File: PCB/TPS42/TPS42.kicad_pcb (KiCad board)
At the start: 2 copper layers, 138.1 x 89.7 mm, 77 parts, among them J1 PJ-320A, J11 Conn_01x06, J14 FH12-10S-0.5SH, J3 TP Sensor Module, J4 TP Module, J6 OLED, J7 TrackPoint, J8 Battery, J9 TP Sensor Module, SW1 SW_DPST_x2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

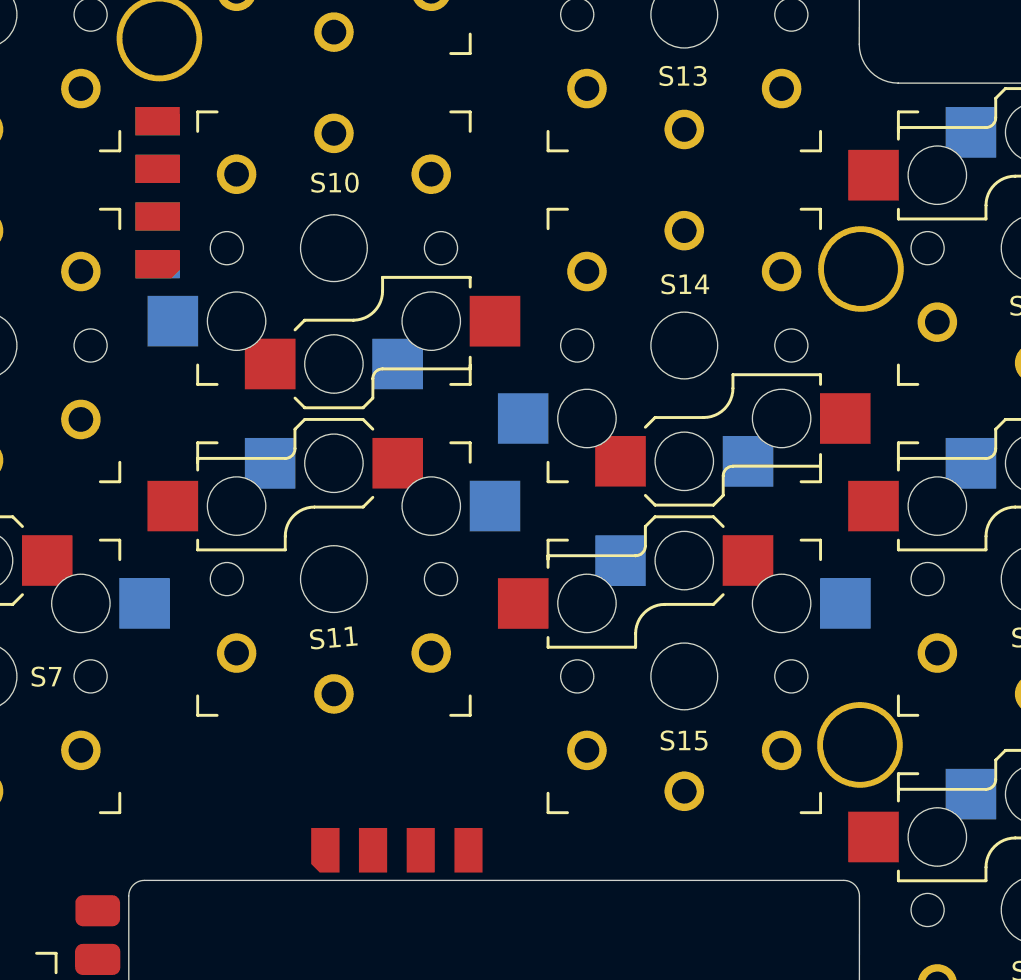
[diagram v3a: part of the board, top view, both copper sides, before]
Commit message: connected tp module
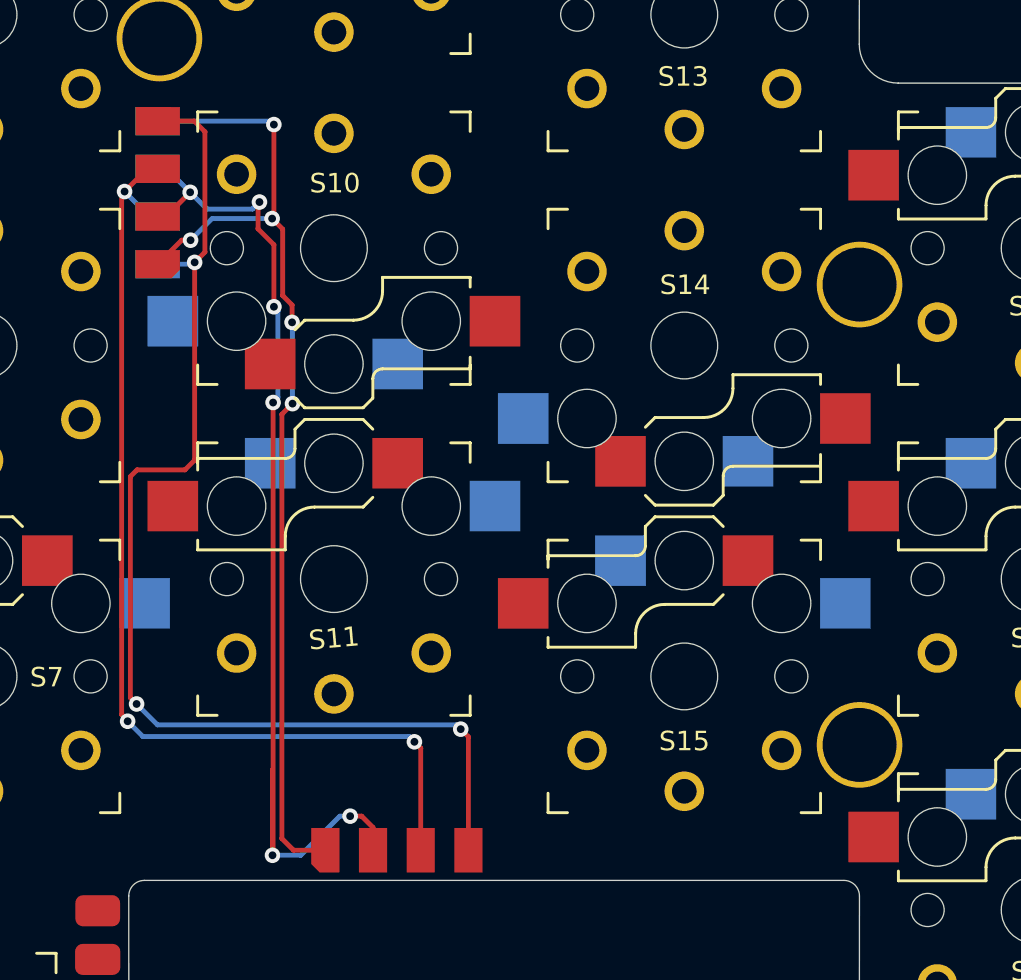
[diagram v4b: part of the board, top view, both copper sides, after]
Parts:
- moved U7 0.80 mm to (175.3, 62.6)
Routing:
- net Net-(J3-Pad4): track 0.00 -> 60.7 mm, vias 0 -> 3
- net Net-(J3-Pad2): track 0.00 -> 54.4 mm, vias 0 -> 6
- net Net-(J3-Pad3): track 0.00 -> 53.9 mm, vias 0 -> 3
- net Net-(J3-Pad1): track 0.00 -> 52.8 mm, vias 0 -> 5
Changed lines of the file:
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@@
   )
   (footprint "TPS42:HOLE_M2_TH" (layer "F.Cu")
-    (at 175.35 61.82)
+    (at 175.28 62.62)
     (property "Sheetfile" "TPS42.kicad_sch")
     (property "Sheetname" "")
@@
   )
   (footprint "TPS42:HOLE_M2_TH" (layer "F.Cu")
-    (at 175.3 86.27)
+    (at 175.28 86.27)
     (property "Sheetfile" "TPS42.kicad_sch")
     (property "Sheetname" "")
@@
     (effects (font (size 1 1) (thickness 0.15)))
   )
+  (segment (start 140.455 60.34) (end 139.22 61.575) (width 0.25) (layer "F.Cu") (net 44))
+  (segment (start 146.1245 63.667517) (end 145.641889 63.184906) (width 0.25) (layer "F.Cu") (net 44))
+  (segment (start 145.19 59.14) (end 145.1 59.23) (width 0.25) (layer "F.Cu") (net 44))
+  (segment (start 145.59952 69.285684) (end 145.59952 91.07952) (width 0.25) (layer "F.Cu") (net 44))
+  (segment (start 145.641889 59.771889) (end 145.1 59.23) (width 0.25) (layer "F.Cu") (net 44))
+  (segment (start 146.147856 68.737348) (end 145.59952 69.285684) (width 0.25) (layer "F.Cu") (net 44))
+  (segment (start 140.91 60.34) (end 140.455 60.34) (width 0.25) (layer "F.Cu") (net 44))
+  (segment (start 145.59952 91.07952) (end 146.2 91.68) (width 0.25) (layer "F.Cu") (net 44))
+  (segment (start 145.19 54.4) (end 145.19 59.14) (width 0.25) (layer "F.Cu") (net 44))
+  (segment (start 146.1245 64.56) (end 146.1245 63.667517) (width 0.25) (layer "F.Cu") (net 44))
+  (segment (start 146.2 91.68) (end 147.835 91.68) (width 0.25) (layer "F.Cu") (net 44))
+  (segment (start 145.641889 63.184906) (end 145.641889 59.771889) (width 0.25) (layer "F.Cu") (net 44))
+  (via (at 146.1245 64.56) (size 0.8) (drill 0.4) (layers "F.Cu" "B.Cu") (net 44))
+  (via (at 145.19 54.4) (size 0.8) (drill 0.4) (layers "F.Cu" "B.Cu") (net 44))
+  (via (at 140.91 60.34) (size 0.8) (drill 0.4) (layers "F.Cu" "B.Cu") (net 44))
+  (via (at 145.1 59.23) (size 0.8) (drill 0.4) (layers "F.Cu" "B.Cu") (net 44))
+  (via (at 146.147856 68.737348) (size 0.8) (drill 0.4) (layers "F.Cu" "B.Cu") (net 44))
+  (segment (start 145.015 54.225) (end 145.19 54.4) (width 0.25) (layer "B.Cu") (net 44))
+  (segment (start 142.02 59.23) (end 145.1 59.23) (width 0.25) (layer "B.Cu") (net 44))
+  (segment (start 139.22 54.225) (end 145.015 54.225) (width 0.25) (layer "B.Cu") (net 44))
+  (segment (start 140.91 60.34) (end 142.02 59.23) (width 0.25) (layer "B.Cu") (net 44))
+  (segment (start 146.14 68.729492) (end 146.14 64.5755) (width 0.25) (layer "B.Cu") (net 44))
+  (segment (start 146.14 64.5755) (end 146.1245 64.56) (width 0.25) (layer "B.Cu") (net 44))
+  (segment (start 146.147856 68.737348) (end 146.14 68.729492) (width 0.25) (layer "B.Cu") (net 44))
+  (segment (start 144.375489 58.454511) (end 144.45 58.38) (width 0.25) (layer "F.Cu") (net 45))
+  (segment (start 149.7 89.93) (end 150.285 90.515) (width 0.25) (layer "F.Cu") (net 45))
+  (segment (start 150.285 90.515) (end 150.285 91.68) (width 0.25) (layer "F.Cu") (net 45))
+  (segment (start 145.12 91.94) (end 145.12 87.53) (width 0.25) (layer "F.Cu") (net 45))
+  (segment (start 145.15 68.68) (end 145.15 91.91) (width 0.25) (layer "F.Cu") (net 45))
+  (segment (start 145.15 91.91) (end 145.12 91.94) (width 0.25) (layer "F.Cu") (net 45))
+  (segment (start 140.89 57.88) (end 139.645 59.125) (width 0.25) (layer "F.Cu") (net 45))
+  (segment (start 149.11 89.93) (end 149.7 89.93) (width 0.25) (layer "F.Cu") (net 45))
+  (segment (start 145.192369 60.572369) (end 144.375489 59.755489) (width 0.25) (layer "F.Cu") (net 45))
+  (segment (start 139.645 59.125) (end 139.22 59.125) (width 0.25) (layer "F.Cu") (net 45))
+  (segment (start 145.192369 63.76) (end 145.192369 60.572369) (width 0.25) (layer "F.Cu") (net 45))
+  (segment (start 144.375489 59.755489) (end 144.375489 58.454511) (width 0.25) (layer "F.Cu") (net 45))
+  (via (at 144.45 58.38) (size 0.8) (drill 0.4) (layers "F.Cu" "B.Cu") (net 45))
+  (via (at 145.192369 63.76) (size 0.8) (drill 0.4) (layers "F.Cu" "B.Cu") (net 45))
+  (via (at 140.89 57.88) (size 0.8) (drill 0.4) (layers "F.Cu" "B.Cu") (net 45))
+  (via (at 145.15 68.68) (size 0.8) (drill 0.4) (layers "F.Cu" "B.Cu") (net 45))
+  (via (at 145.12 91.94) (size 0.8) (drill 0.4) (layers "F.Cu" "B.Cu") (net 45))
+  (via (at 149.11 89.93) (size 0.8) (drill 0.4) (layers "F.Cu" "B.Cu") (net 45))
+  (segment (start 148.58 89.93) (end 146.57 91.94) (width 0.25) (layer "B.Cu") (net 45))
+  (segment (start 146.57 91.94) (end 145.12 91.94) (width 0.25) (layer "B.Cu") (net 45))
+  (segment (start 145.192369 63.76) (end 145.4 63.967631) (width 0.25) (layer "B.Cu") (net 45))
+  (segment (start 144.09 58.74) (end 144.45 58.38) (width 0.25) (layer "B.Cu") (net 45))
+  (segment (start 149.11 89.93) (end 148.58 89.93) (width 0.25) (layer "B.Cu") (net 45))
+  (segment (start 140.89 57.88) (end 141.75 58.74) (width 0.25) (layer "B.Cu") (net 45))
+  (segment (start 145.4 63.967631) (end 145.4 68.43) (width 0.25) (layer "B.Cu") (net 45))
+  (segment (start 141.75 58.74) (end 144.09 58.74) (width 0.25) (layer "B.Cu") (net 45))
+  (segment (start 139.685 56.675) (end 139.22 56.675) (width 0.25) (layer "B.Cu") (net 45))
+  (segment (start 145.4 68.43) (end 145.15 68.68) (width 0.25) (layer "B.Cu") (net 45))
+  (segment (start 140.89 57.88) (end 139.685 56.675) (width 0.25) (layer "B.Cu") (net 45))
+  (segment (start 139.865 56.675) (end 139.22 56.675) (width 0.25) (layer "F.Cu") (net 46))
+  (segment (start 152.41 86.11) (end 152.735 86.435) (width 0.25) (layer "F.Cu") (net 46))
+  (segment (start 137.37 57.99) (end 137.52 57.84) (width 0.25) (layer "F.Cu") (net 46))
+  (segment (start 137.37 84.708564) (end 137.37 57.99) (width 0.25) (layer "F.Cu") (net 46))
+  (segment (start 152.735 86.435) (end 152.735 91.68) (width 0.25) (layer "F.Cu") (net 46))
+  (segment (start 137.52 57.84) (end 138.685 56.675) (width 0.25) (layer "F.Cu") (net 46))
+  (segment (start 137.677064 85.015628) (end 137.37 84.708564) (width 0.25) (layer "F.Cu") (net 46))
+  (segment (start 138.685 56.675) (end 139.22 56.675) (width 0.25) (layer "F.Cu") (net 46))
+  (segment (start 137.677064 85.053399) (end 137.677064 85.015628) (width 0.25) (layer "F.Cu") (net 46))
+  (via (at 137.677064 85.053399) (size 0.8) (drill 0.4) (layers "F.Cu" "B.Cu") (net 46))
+  (via (at 137.52 57.84) (size 0.8) (drill 0.4) (layers "F.Cu" "B.Cu") (net 46))
+  (via (at 152.41 86.11) (size 0.8) (drill 0.4) (layers "F.Cu" "B.Cu") (net 46))
+  (segment (start 138.463665 85.84) (end 137.677064 85.053399) (width 0.25) (layer "B.Cu") (net 46))
+  (segment (start 138.805 59.125) (end 139.22 59.125) (width 0.25) (layer "B.Cu") (net 46))
+  (segment (start 152.41 86.11) (end 152.14 85.84) (width 0.25) (layer "B.Cu") (net 46))
+  (segment (start 152.14 85.84) (end 138.463665 85.84) (width 0.25) (layer "B.Cu") (net 46))
+  (segment (start 139.22 59.125) (end 139.825 59.125) (width 0.25) (layer "B.Cu") (net 46))
+  (segment (start 137.52 57.84) (end 138.805 59.125) (width 0.25) (layer "B.Cu") (net 46))
+  (segment (start 139.643 54.22) (end 141.1 54.22) (width 0.25) (layer "F.Cu") (net 47))
+  (segment (start 138.16 72.14) (end 140.62 72.14) (width 0.25) (layer "F.Cu") (net 47))
+  (segment (start 140.62 72.14) (end 141.12 71.64) (width 0.25) (layer "F.Cu") (net 47))
+  (segment (start 141.65 54.77) (end 141.65 60.95) (width 0.25) (layer "F.Cu") (net 47))
+  (segment (start 154.79 85.46) (end 155.185 85.855) (width 0.25) (layer "F.Cu") (net 47))
+  (segment (start 141.1 54.22) (end 141.65 54.77) (width 0.25) (layer "F.Cu") (net 47))
+  (segment (start 137.81952 83.848125) (end 137.81952 72.48048) (width 0.25) (layer "F.Cu") (net 47))
+  (segment (start 141.65 60.95) (end 141.12 61.48) (width 0.25) (layer "F.Cu") (net 47))
+  (segment (start 155.185 85.855) (end 155.185 91.68) (width 0.25) (layer "F.Cu") (net 47))
+  (segment (start 137.81952 72.48048) (end 138.16 72.14) (width 0.25) (layer "F.Cu") (net 47))
+  (segment (start 138.137836 84.166441) (end 137.81952 83.848125) (width 0.25) (layer "F.Cu") (net 47))
+  (segment (start 139.22 54.225) (end 139.638 54.225) (width 0.25) (layer "F.Cu") (net 47))
+  (segment (start 141.12 71.64) (end 141.12 61.48) (width 0.25) (layer "F.Cu") (net 47))
+  (segment (start 139.638 54.225) (end 139.643 54.22) (width 0.25) (layer "F.Cu") (net 47))
+  (via (at 154.79 85.46) (size 0.8) (drill 0.4) (layers "F.Cu" "B.Cu") (net 47))
+  (via (at 141.12 61.48) (size 0.8) (drill 0.4) (layers "F.Cu" "B.Cu") (net 47))
+  (via (at 138.137836 84.166441) (size 0.8) (drill 0.4) (layers "F.Cu" "B.Cu") (net 47))
+  (segment (start 154.57 85.24) (end 139.211395 85.24) (width 0.25) (layer "B.Cu") (net 47))
+  (segment (start 154.79 85.46) (end 154.57 85.24) (width 0.25) (layer "B.Cu") (net 47))
+  (segment (start 139.22 61.575) (end 141.025 61.575) (width 0.25) (layer "B.Cu") (net 47))
+  (segment (start 139.211395 85.24) (end 138.137836 84.166441) (width 0.25) (layer "B.Cu") (net 47))
+  (segment (start 141.025 61.575) (end 141.12 61.48) (width 0.25) (layer "B.Cu") (net 47))
   (group "" (id 50fe513a-550e-4e47-b3e6-31ef45e7540b)
     (members

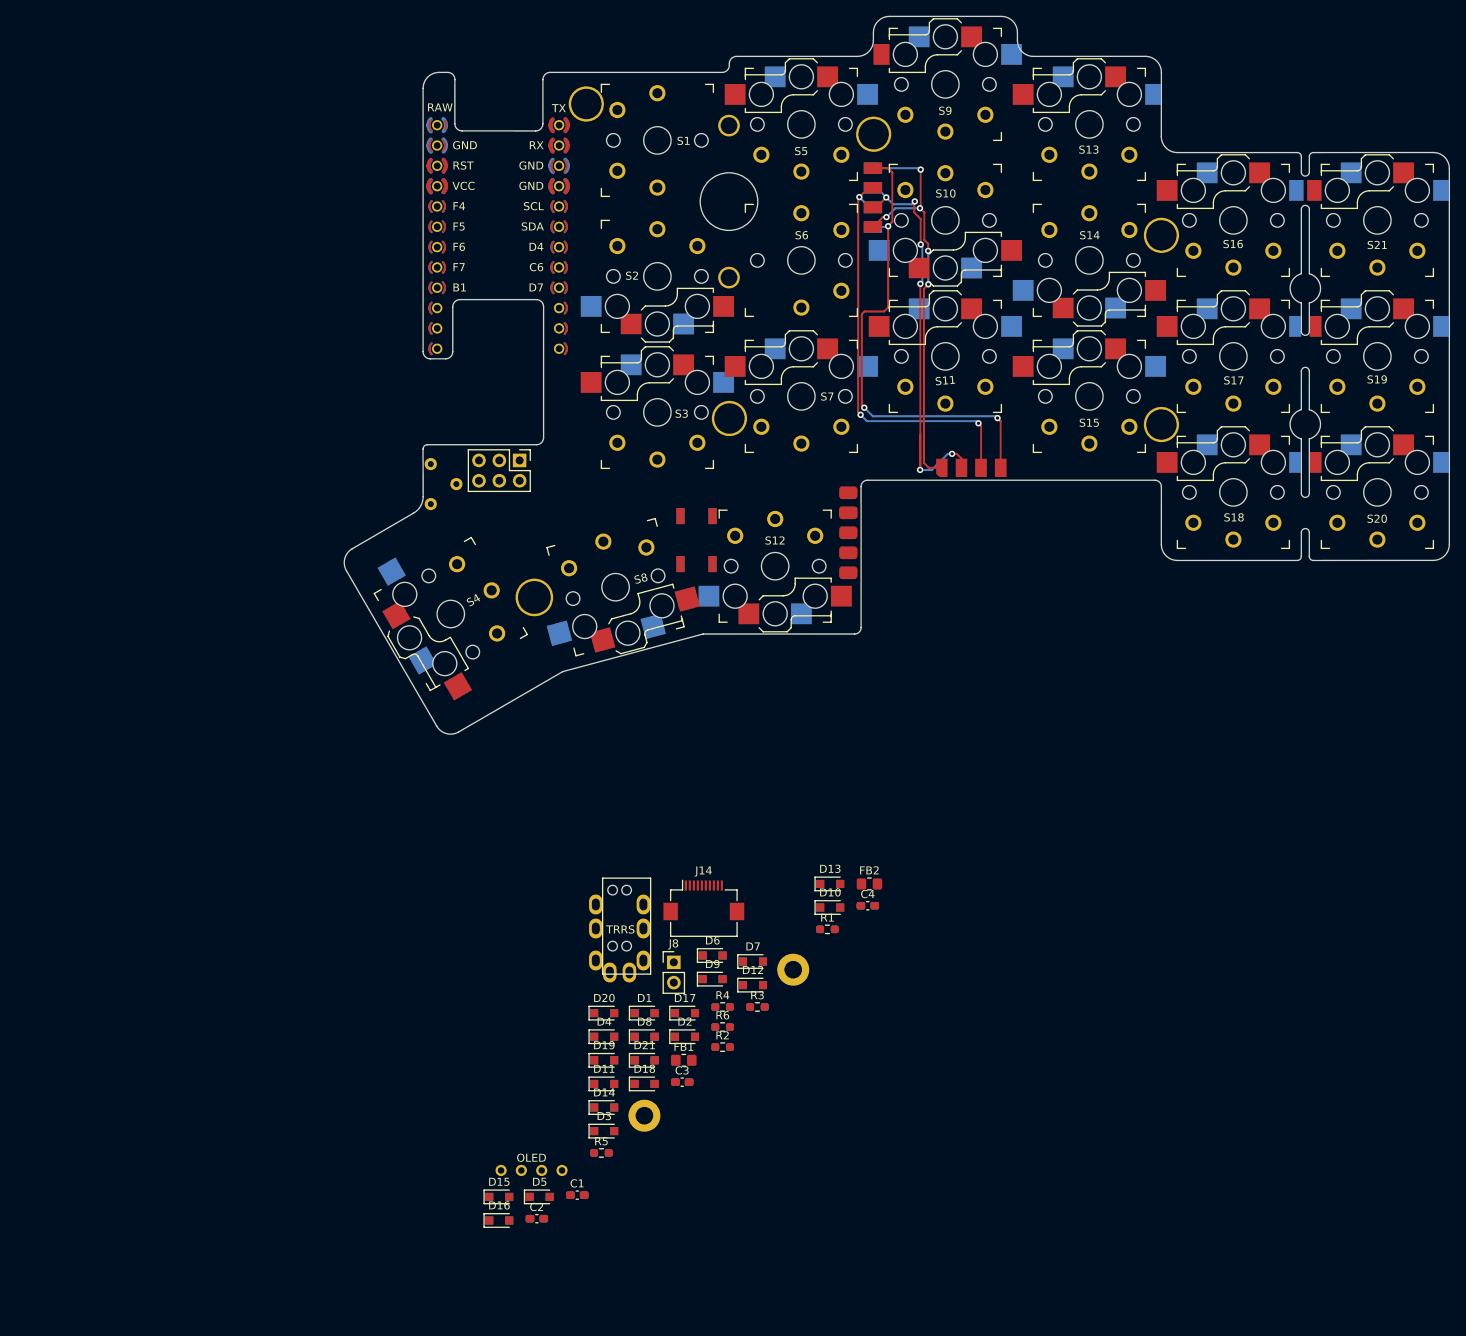
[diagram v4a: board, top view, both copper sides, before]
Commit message: place components
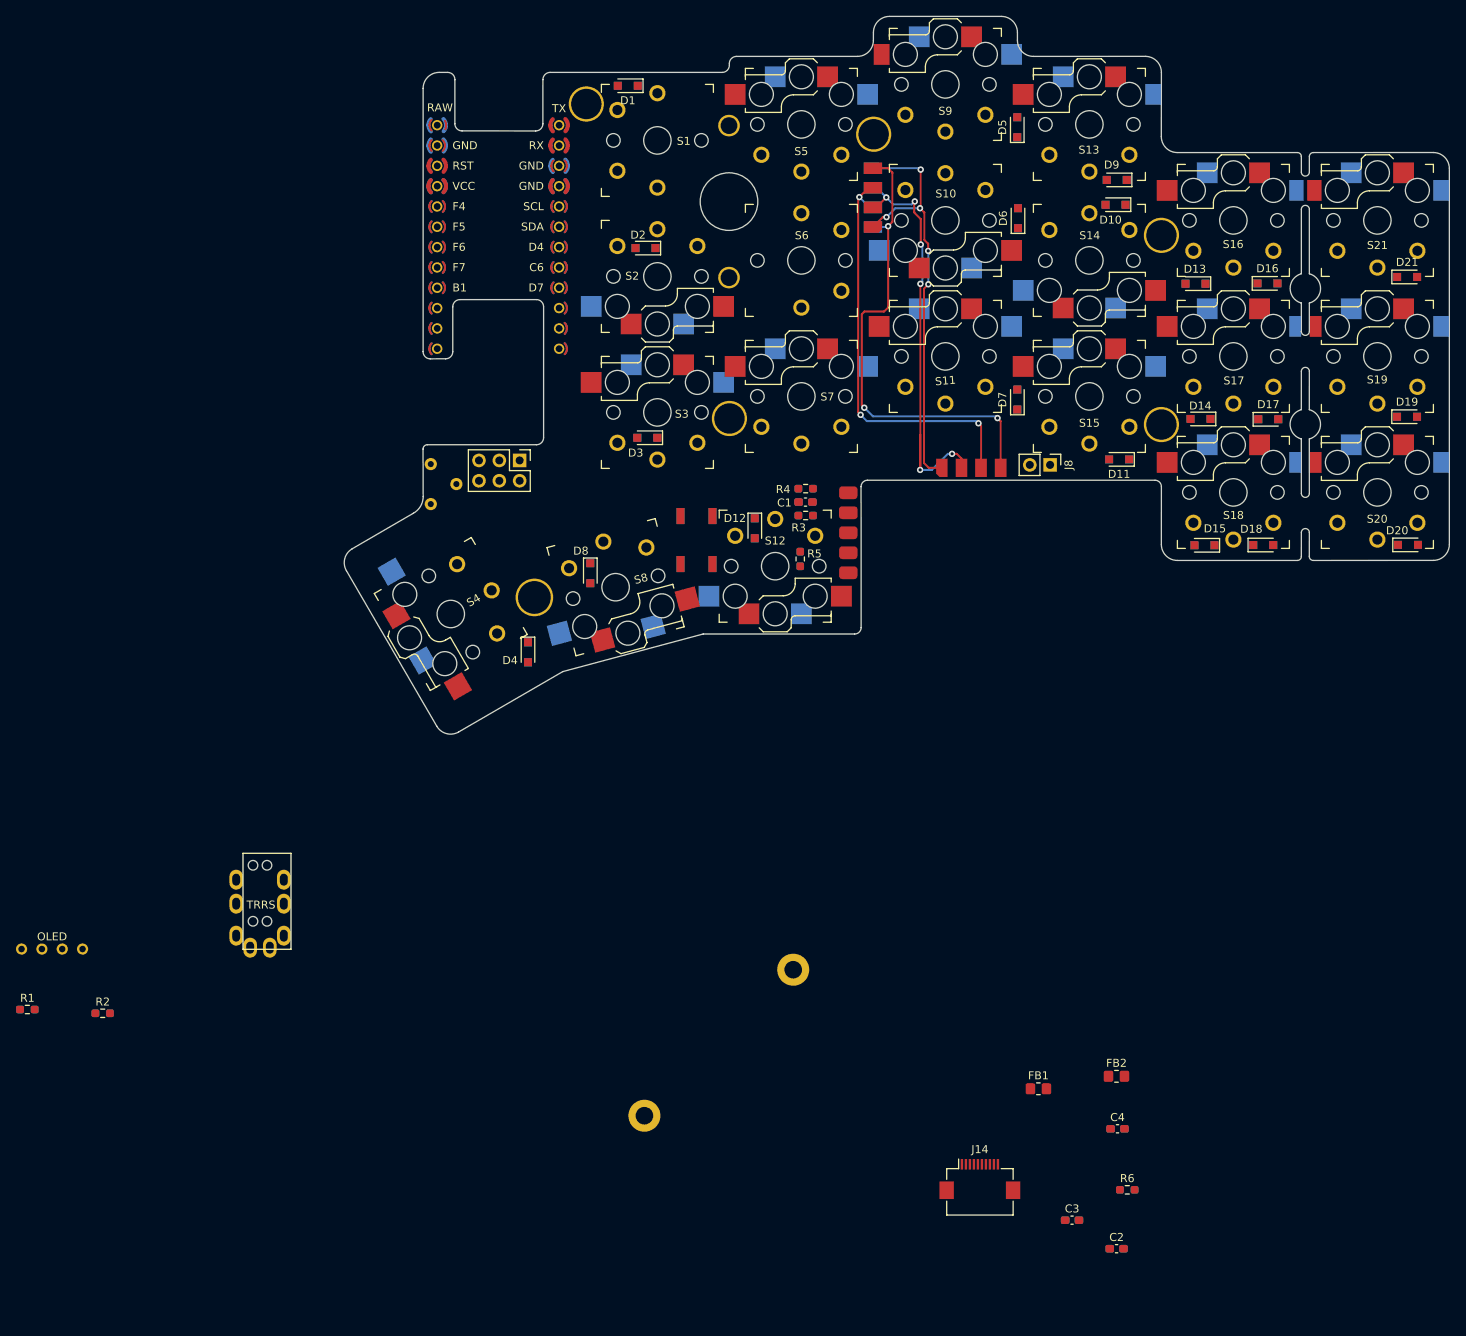
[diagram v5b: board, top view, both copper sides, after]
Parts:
- moved D16 151.5 mm to (188.5, 68.6)
- moved D5 146.4 mm to (157.3, 49.1), turned to 90 degrees
- moved D21 136.6 mm to (206.0, 67.8)
- moved D19 128.6 mm to (206.0, 85.3)
- moved D15 120.0 mm to (180.7, 101.4), turned to 180 degrees
- moved D20 116.3 mm to (206.1, 101.3)
- moved D1 115.9 mm to (108.6, 43.9), turned to 180 degrees
- moved D14 113.9 mm to (180.2, 85.6), turned to 180 degrees
- moved D9 111.9 mm to (169.7, 55.7), turned to 180 degrees
- moved D17 104.0 mm to (188.6, 85.6)
- moved D18 102.6 mm to (188.0, 101.3)
- moved D11 101.2 mm to (170.0, 90.6), turned to 180 degrees
- moved R1 100.5 mm to (33.5, 159.4)
- moved D6 99.8 mm to (157.3, 60.5), turned to 90 degrees
- moved D2 98.7 mm to (110.8, 64.2), turned to 180 degrees
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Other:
- board text added: "C1"
- board text added: "R3"
- board text added: "R4"
- board text added: "R5"
